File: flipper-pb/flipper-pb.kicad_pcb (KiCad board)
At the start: 2 copper layers, 78.7 x 32.4 mm, 160 parts, among them J1 SWD, J2 UART, J3 LEDS_PWR, J4 UART_PWR, U1 FlipperZero, U2 FlipperZero, X1 SolderPad, X10 SolderPad, X11 SolderPad, X12 SolderPad, X13 SolderPad, X14 SolderPad, X15 SolderPad, X16 SolderPad, X17 SolderPad, X18 SolderPad, X19 SolderPad, X2 SolderPad, X20 SolderPad, X21 SolderPad, X22 SolderPad, X23 SolderPad, X24 SolderPad, X25 SolderPad, X26 SolderPad, X27 SolderPad, X28 SolderPad, X29 SolderPad, X3 SolderPad, X30 SolderPad, X31 SolderPad, X4 SolderPad, X5 SolderPad, X6 SolderPad, X7 SolderPad, X8 SolderPad, X9 SolderPad

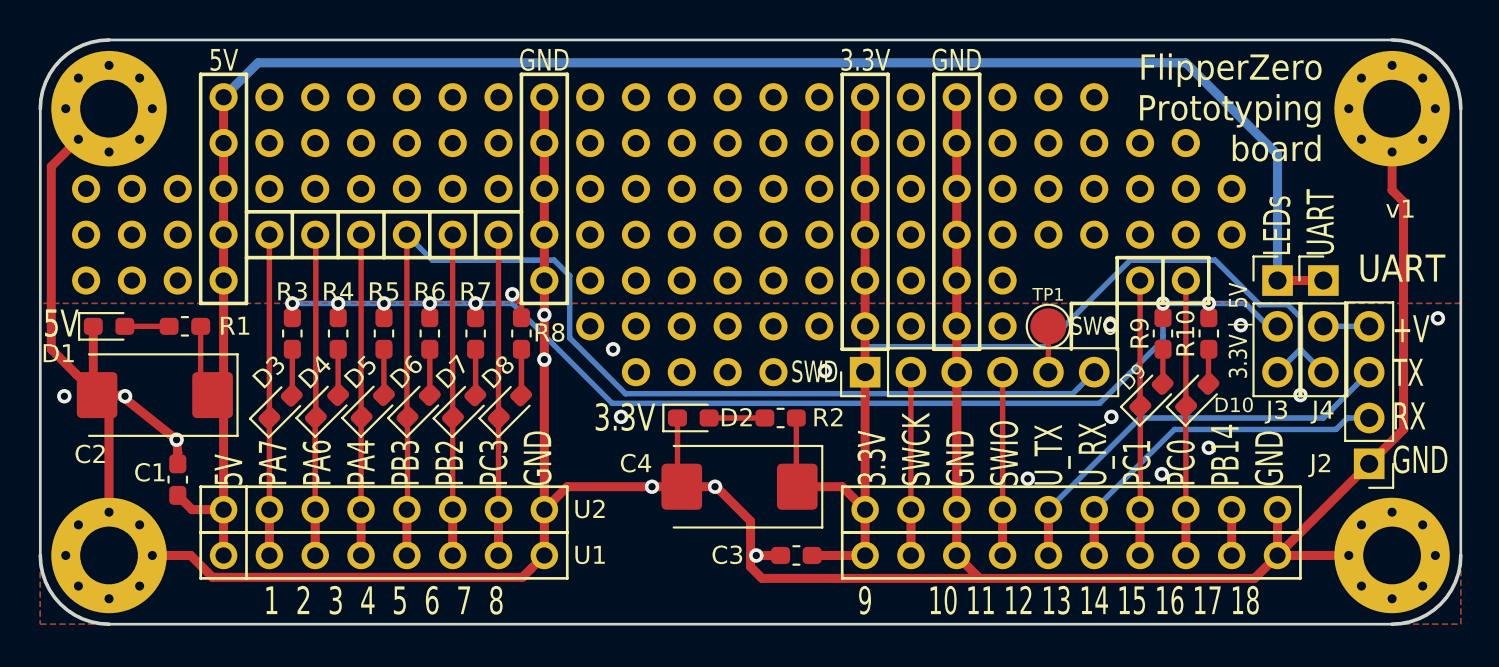
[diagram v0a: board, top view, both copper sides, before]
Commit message: Update with KiCad 9.0
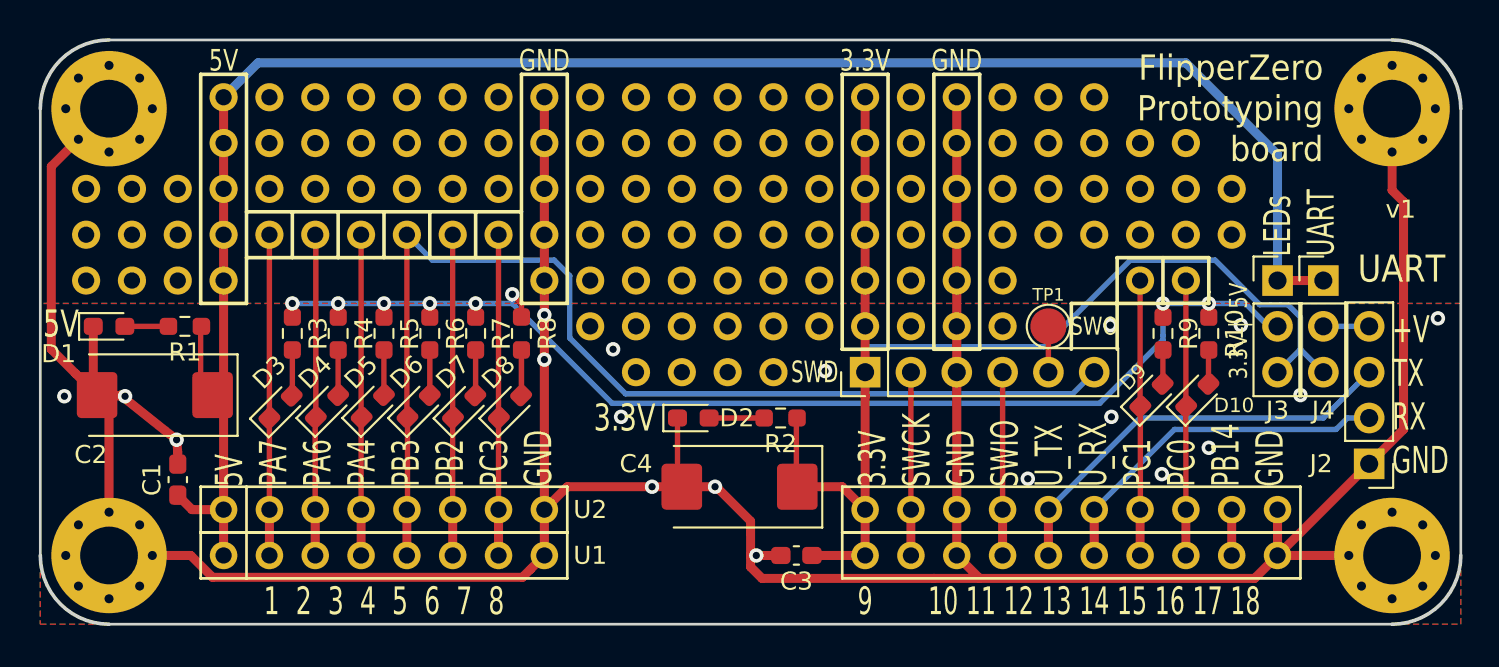
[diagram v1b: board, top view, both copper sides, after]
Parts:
- C1, C3: footprint Capacitor_SMD:C_0603_1608Metric_Pad1.05x0.95mm_HandSolder -> Capacitor_SMD:C_0603_1608Metric_Pad1.08x0.95mm_HandSolder
- R1, R10, R2, R3, R4, R5, R6, R7, R8, R9: footprint Resistor_SMD:R_0603_1608Metric_Pad1.05x0.95mm_HandSolder -> Resistor_SMD:R_0603_1608Metric_Pad0.98x0.95mm_HandSolder
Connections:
- X1 pad 1: (no net) -> unconnected-(X1-Pad1) (x95)
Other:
- net class Default removed

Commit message: Diverse Änderungen
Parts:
- removed D10, D9: LED, LED_SMD:LED_0603_1608Metric_Pad1.05x0.95mm_HandSolder
- removed the X1 at (111.8, 53.3)
- removed the X1 at (111.8, 58.4)
- removed the X1 at (106.7, 63.5)
- removed the X1 at (106.7, 61.0)
- removed the X1 at (116.8, 55.9)
- removed the X1 at (114.3, 55.9)
- removed the X1 at (114.3, 58.4)
- removed the X1 at (119.4, 55.9)
- removed the X1 at (116.8, 58.4)
- removed the X1 at (114.3, 53.3)
- removed the X1 at (116.8, 53.3)
- removed the X1 at (109.2, 50.8)
- removed the X1 at (119.4, 58.4)
- removed the X1 at (111.8, 50.8)
- removed the X1 at (83.8, 58.4)
- removed the X1 at (83.8, 55.9)
- removed the X1 at (83.8, 53.3)
- removed the X1 at (83.8, 50.8)
- removed the X1 at (86.4, 55.9)
- removed the X1 at (109.2, 53.3)
- removed the X1 at (86.4, 58.4)
- removed the X1 at (86.4, 53.3)
- removed the X1 at (86.4, 50.8)
- removed the X1 at (88.9, 58.4)
- removed the X1 at (88.9, 55.9)
- removed the X1 at (88.9, 53.3)
- removed the X1 at (88.9, 50.8)
- removed the X1 at (106.7, 53.3)
- removed the X1 at (91.4, 55.9)
- removed the X1 at (91.4, 58.4)
- removed the X1 at (106.7, 50.8)
- removed the X1 at (106.7, 55.9)
- removed the X1 at (76.2, 53.3)
- removed the X1 at (78.7, 53.3)
- removed the X1 at (109.2, 55.9)
- removed the X1 at (76.2, 50.8)
- removed the X1 at (78.7, 50.8)
- removed the X1 at (106.7, 58.4)
- removed the X1 at (101.6, 50.8)
- removed the X1 at (101.6, 55.9)
- removed the X1 at (101.6, 58.4)
- removed the X1 at (101.6, 53.3)
- removed the X1 at (101.6, 61.0)
- removed the X1 at (109.2, 58.4)
- removed the X1 at (101.6, 63.5)
- removed the X1 at (111.8, 55.9)
- added C5: 100nF, Capacitor_SMD:C_0603_1608Metric_Pad1.08x0.95mm_HandSolder, F.Cu at (106.0, 59.9)
- added C6: 10uF, Capacitor_SMD:C_0603_1608Metric_Pad1.08x0.95mm_HandSolder, F.Cu at (104.3, 59.9)
- added PMOD1: PMOD-Device-x2-Type-1A-GPIO, pmod-conn_6x2:pmod_pin_array_6x2, F.Cu at (85.1, 52.1)
- added PMOD2: PMOD-Device-x2-Type-4A-Expanded-UART, pmod-conn_6x2:pmod_pin_array_6x2, F.Cu at (105.4, 52.1)
- added U3: IIS2DLPCTR, Package_LGA:LGA-12_2x2mm_P0.5mm, F.Cu at (109.3, 59.9)
- added U4: ISM330DHCX, Package_LGA:LGA-14_3x2.5mm_P0.5mm_LayoutBorder3x4y, F.Cu at (109.3, 56.4)
- added X32: SolderPad, lomalkin_kicad_footprints:Flipper-SolderPad, F.Cu at (86.4, 58.4)
- added X33: SolderPad, lomalkin_kicad_footprints:Flipper-SolderPad, F.Cu at (83.8, 58.4)
- R10, R9: value 1K -> 10K
- moved X26 20.9 mm to (83.8, 55.9)
- moved X25 18.0 mm to (86.4, 55.9)
- moved X1 15.2 mm to (76.2, 53.3)
- moved X1 15.2 mm to (76.2, 50.8)
- moved X28 12.7 mm to (91.4, 58.4)
- moved X20 11.4 mm to (88.9, 55.9)
- moved R9 10.4 mm to (116.1, 53.5), turned to 90 degrees
- moved R10 10.4 mm to (117.7, 53.5)
- moved X29 9.16 mm to (88.9, 58.4)
- moved X19 8.03 mm to (91.4, 55.9)
- moved X21 2.54 mm to (101.6, 61.0)
- moved X22 2.54 mm to (101.6, 55.9)
- moved X23 2.54 mm to (101.6, 63.5)
- moved X24 2.54 mm to (101.6, 58.4)
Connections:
- R10 pad 1: Net-(J3-Pin_2) -> /3.3V
- R10 pad 2: Net-(D10-A) -> Net-(U3-CS)
- R9 pad 1: Net-(J3-Pin_2) -> Net-(U3-CS)
- R9 pad 2: Net-(D9-A) -> GND
- X19 pad 1: /3.3V -> Net-(PMOD1-IOA0)
- X20 pad 1: /3.3V -> Net-(PMOD1-IOA1)
- X25 pad 1: GND -> Net-(PMOD1-IOA2)
- X26 pad 1: GND -> Net-(PMOD1-IOA3)
- X28 pad 1: GND -> Net-(PMOD1-IOB0)
- X29 pad 1: GND -> Net-(PMOD1-IOB1)
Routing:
- net /PA6: track 17.8 -> 96.9 mm, vias 0 -> 3
- net /PA4: track 17.8 -> 73.5 mm, vias 0 -> 3
- net /PA7: track 17.8 -> 71.3 mm
- net /3.3V: track 70.5 -> 123.3 mm, vias 0 -> 4
- net /PC3: track 17.8 -> 59.6 mm
- net /UART_RX: track 19.9 -> 57.4 mm
- net /UART_TX: track 23.5 -> 54.6 mm
- net GND: track 203.8 -> 228.5 mm
- net /SWO: track 62.1 -> 80.0 mm, vias 0 -> 2
- net /PC1: track 15.3 -> 33.0 mm, vias 0 -> 1
- net Net-(U3-CS): track 0.00 -> 17.5 mm, vias 0 -> 2
- net /PC0: track 15.3 -> 32.3 mm, vias 0 -> 1
- net Net-(PMOD1-IOB3): track 0.00 -> 8.68 mm
- net Net-(PMOD1-IOB0): track 0.00 -> 8.67 mm
- net Net-(PMOD1-IOB2): track 0.00 -> 8.65 mm
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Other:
- rule pad_to_mask_clearance: 0.051 -> 0.038
- board text added: "FlipperZero Sensorboard"
- board text removed: "FlipperZero Prototyping board"
- board text removed: "GND"

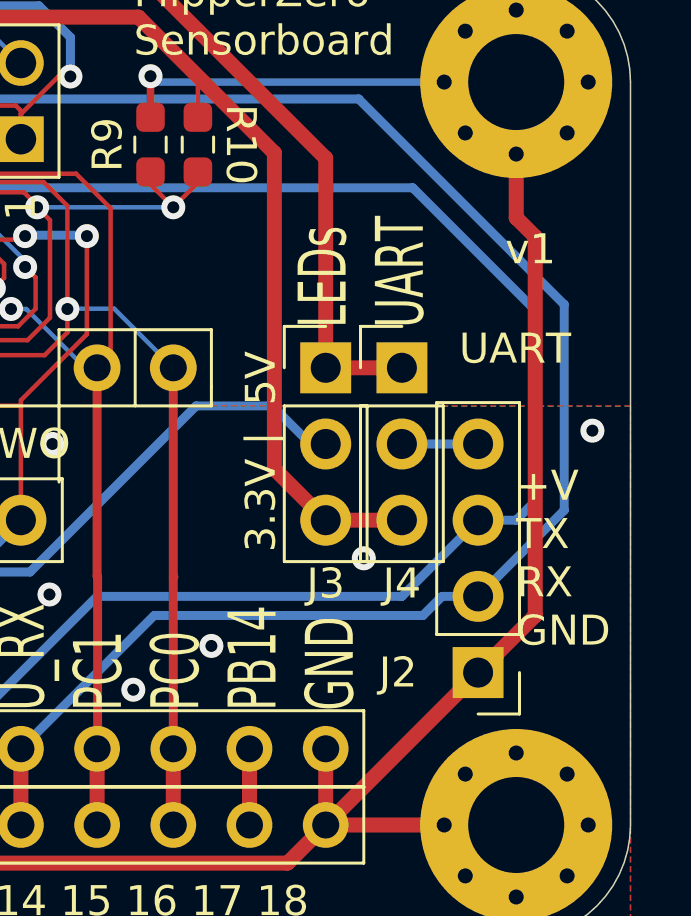
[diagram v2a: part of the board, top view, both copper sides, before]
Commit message: Silkscreens korrigiert, 3D-Modelle für PMOD hinzugefügt
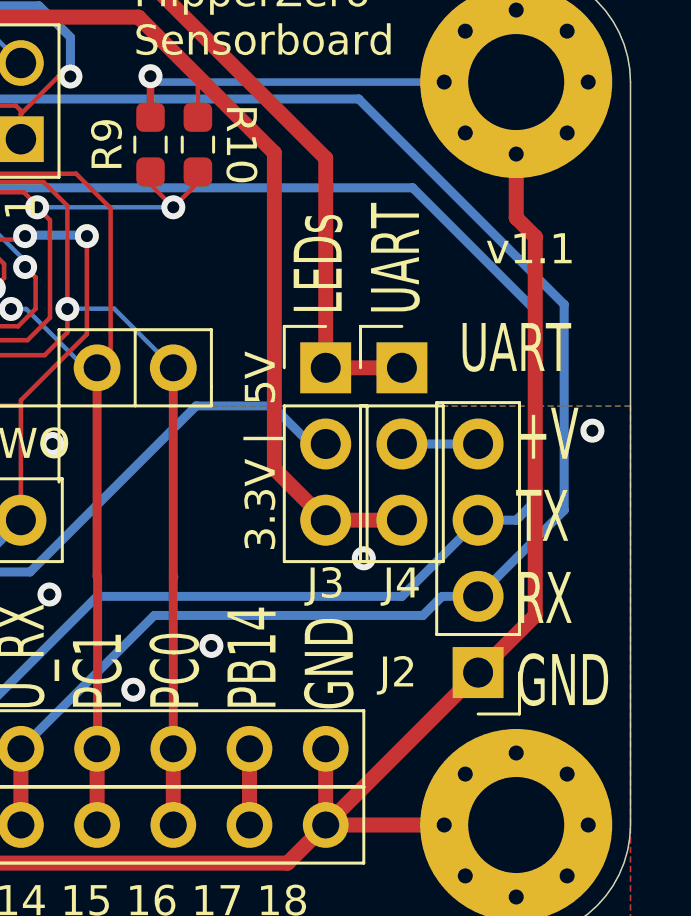
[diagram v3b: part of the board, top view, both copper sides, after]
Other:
- board text added: "v1.1"
- board text removed: "v1"
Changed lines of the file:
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@@
 		)
 		(fp_text user "GND"
-			(at -3.6 3.76 180)
+			(at -3.6 3.76 0)
 			(unlocked yes)
 			(layer "B.SilkS")
@@
 		)
 		(fp_text user "VCC"
-			(at -3.6 6.67 180)
+			(at -3.6 6.67 0)
 			(unlocked yes)
 			(layer "B.SilkS")
@@
 			(rotate
 				(xyz 0 0 180)
+			)
+		)
+		(model "${KICAD9_3DMODEL_DIR}/Connector_PinHeader_2.54mm.3dshapes/PinHeader_2x06_P2.54mm_Horizontal.wrl"
+			(offset
+				(xyz 1.25 -6.35 0)
+			)
+			(scale
+				(xyz 1 1 1)
+			)
+			(rotate
+				(xyz -0 -0 -180)
 			)
 		)
@@
 		)
 		(fp_text user "VCC"
-			(at -3.6 6.35 180)
+			(at -3.6 6.35 0)
 			(unlocked yes)
 			(layer "B.SilkS")
@@
 			(rotate
 				(xyz 0 0 180)
+			)
+		)
+		(model "${KICAD9_3DMODEL_DIR}/Connector_PinHeader_2.54mm.3dshapes/PinHeader_2x06_P2.54mm_Horizontal.wrl"
+			(offset
+				(xyz 1.25 -6.35 0)
+			)
+			(scale
+				(xyz 1 1 1)
+			)
+			(rotate
+				(xyz -0 -0 -180)
 			)
 		)
@@
 		)
 	)
-	(gr_text "v1"
+	(gr_text "v1.1"
 		(at 128.74752 57.01284 0)
 		(layer "F.SilkS")
@@
 	)
 	(gr_text "LEDs\nUART"
-		(at 123.13 59.63 90)
+		(at 123 59.2 90)
 		(layer "F.SilkS")
 		(effects
@@
 		(effects
 			(font
-				(size 1 1)
+				(size 1.6 1)
 				(thickness 0.153)
 			)
@@
 		(effects
 			(font
-				(size 1 1)
+				(size 1.7 1)
 				(thickness 0.153)
 			)
